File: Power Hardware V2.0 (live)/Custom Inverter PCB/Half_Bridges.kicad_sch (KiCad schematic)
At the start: 27 parts, among them Q1 CSD19532Q5B, Q2 CSD19532Q5B, Q3 CSD19532Q5B, Q4 CSD19532Q5B, Q5 CSD19532Q5B, Q6 CSD19532Q5B

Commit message: switches instead of relays. Short on half bridge fixed. encoder page made. root page connections fixed
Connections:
- net +100VDC: no longer C6.2, C7.2, C8.2, Q1.1, Q2.5_8, Q3.1, Q4.5_8, Q5.1, Q6.5_8, R5.2, R8.2, R9.2, TP1.TP, TP6.TP, TP9.TP
- new net GND: C6.2, C7.2, C8.2, R5.2, R8.2, R9.2
- new net MOTA: Q1.1, Q2.5_8, TP1.TP
- new net MOTB: Q3.1, Q4.5_8, TP6.TP
- new net MOTC: Q5.1, Q6.5_8, TP9.TP

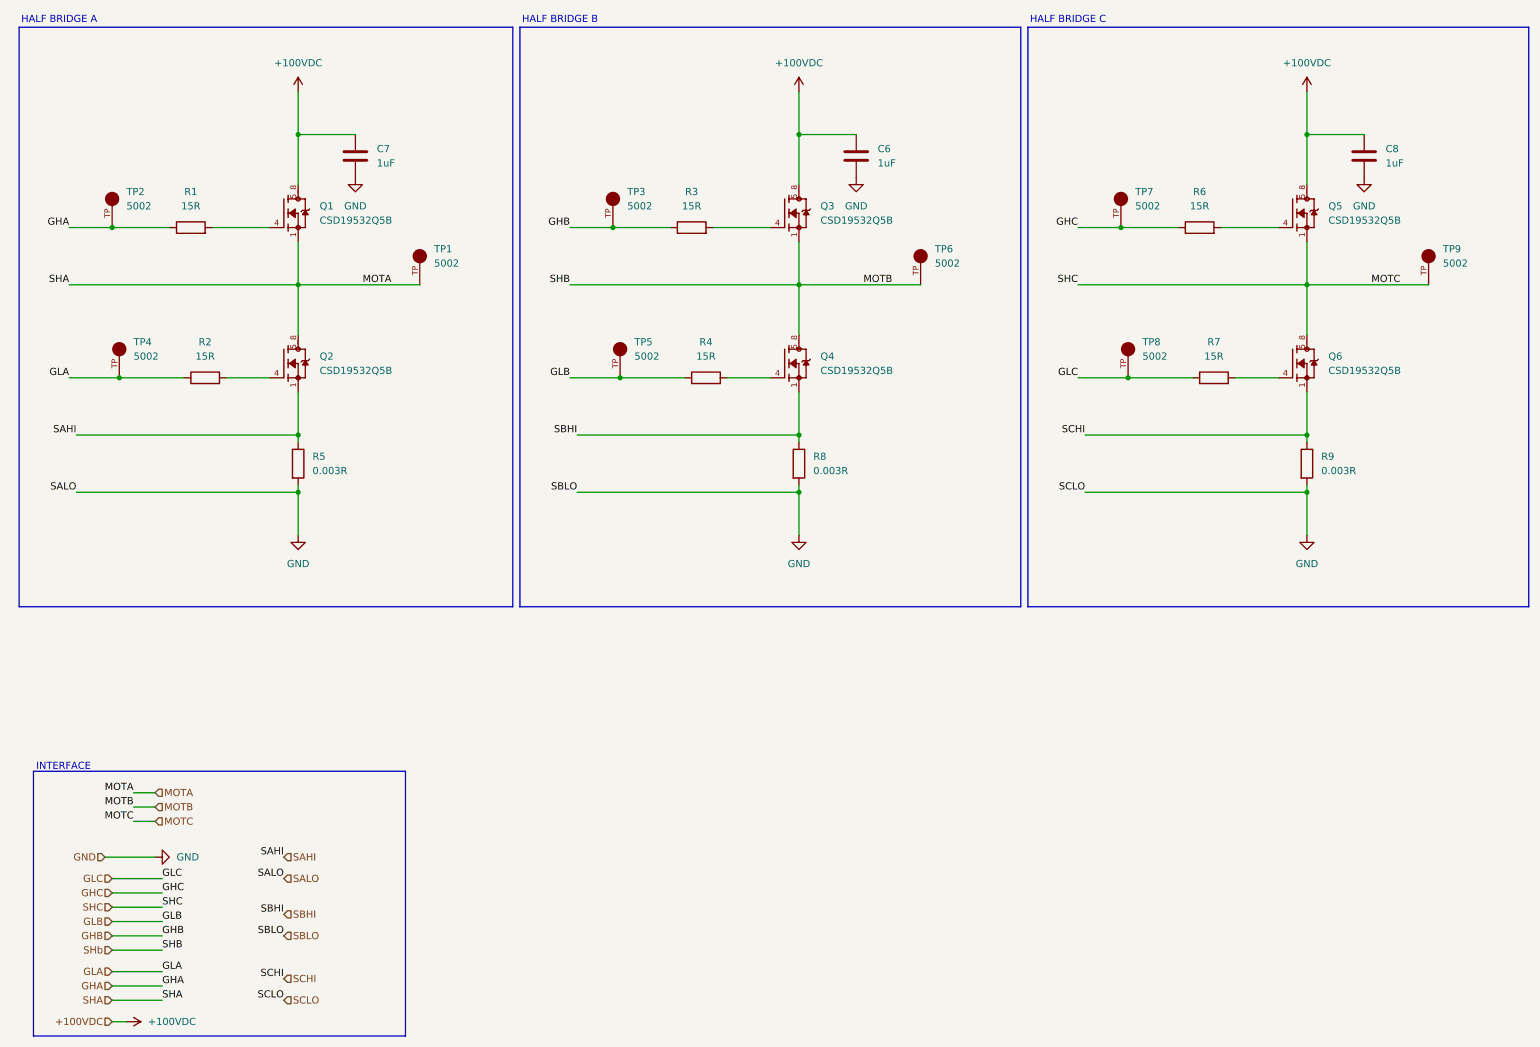
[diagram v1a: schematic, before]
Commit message: Schematic Changes
-Changed 3.3V regulator to a higher power unit for the sin-cos circuit (from 500mA to 3A)
-Fixed flipped MOTA,B,C connection to Output Terminal
- Current Sense IC setup
- Fuses for Phase current outputs
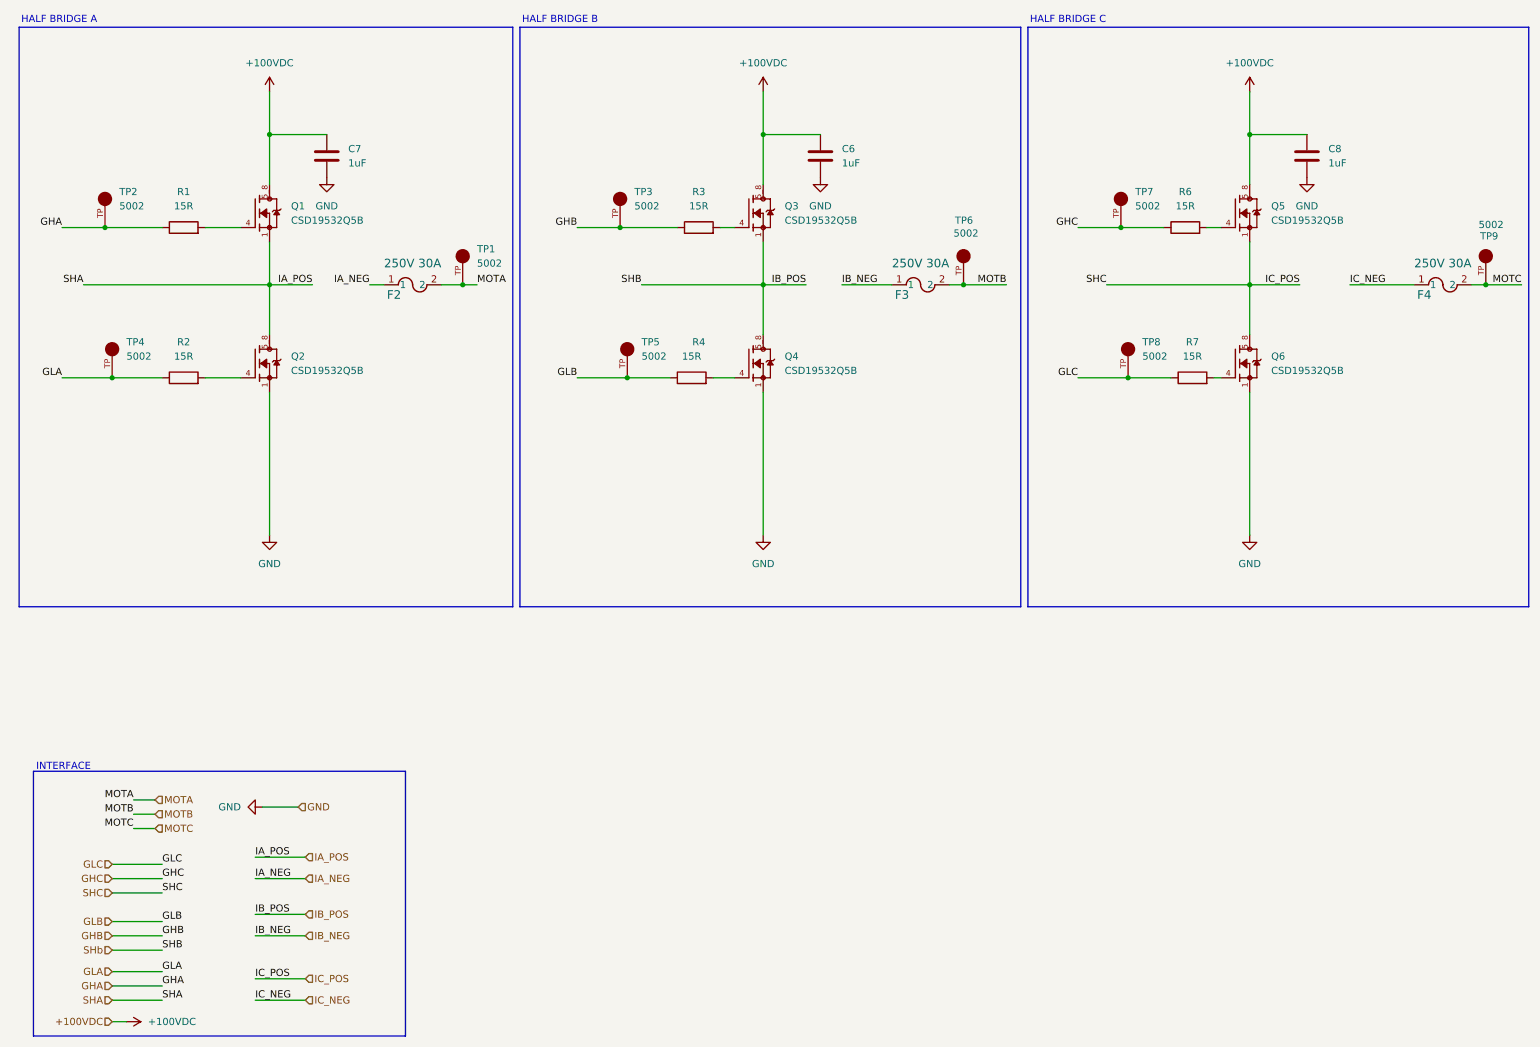
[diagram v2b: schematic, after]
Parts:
- removed R5, R8, R9: 0.003R, Resistor_SMD:R_2512_6332Metric, symbol Device:R
- added F2, F3, F4: 250V 30A, 0463030.ER:FUSE_0463_LTF, symbol 2025-02-24_21-09-15:0463030.ER
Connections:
- net SAHI is gone; now on net GND: Q2.1
- net SBHI is gone; now on net GND: Q4.1
- net SCHI is gone; now on net GND: Q6.1
- net MOTA: now also F2.2; no longer Q1.1, Q2.5_8
- net MOTB: now also F3.2; no longer Q3.1, Q4.5_8
- net MOTC: now also F4.2; no longer Q5.1, Q6.5_8
- new net IA_NEG: F2.1
- new net IA_POS: Q1.1, Q2.5_8
- new net IB_NEG: F3.1
- new net IB_POS: Q3.1, Q4.5_8
- new net IC_NEG: F4.1
- new net IC_POS: Q5.1, Q6.5_8
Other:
- moved on the sheet: C6, C7, C8, Q1, Q2, Q3, Q4, Q5, Q6, R1, R2, R3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

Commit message: no major changes
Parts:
- F2, F3, F4: footprint 0463030.ER:FUSE_0463_LTF -> 0463030ERFUSE:FUSE_0463_LTF-L
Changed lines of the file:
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@@
 			)
 		)
-		(property "Footprint" "0463030.ER:FUSE_0463_LTF"
+		(property "Footprint" "0463030ERFUSE:FUSE_0463_LTF-L"
 			(at 78.74 62.23 0)
 			(effects
@@
 			)
 		)
-		(property "Footprint" "0463030.ER:FUSE_0463_LTF"
+		(property "Footprint" "0463030ERFUSE:FUSE_0463_LTF-L"
 			(at 168.91 62.23 0)
 			(effects
@@
 			)
 		)
-		(property "Footprint" "0463030.ER:FUSE_0463_LTF"
+		(property "Footprint" "0463030ERFUSE:FUSE_0463_LTF-L"
 			(at 261.62 62.23 0)
 			(effects

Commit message: footprint lib fixes
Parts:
- F2, F3, F4: footprint 0463030ERFUSE:FUSE_0463_LTF-L -> 0463030_ER:FUSE_0463_LTF-M
- Q1, Q2, Q3, Q4, Q5, Q6: footprint CSD19532Q5B (1):TRANS_CSD19532Q5B -> CSD19532Q5B:TRANS_CSD19532Q5B
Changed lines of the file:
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@@
 			)
 		)
-		(property "Footprint" "0463030ERFUSE:FUSE_0463_LTF-L"
+		(property "Footprint" "0463030_ER:FUSE_0463_LTF-M"
 			(at 78.74 62.23 0)
 			(effects
@@
 			)
 		)
-		(property "Footprint" "CSD19532Q5B (1):TRANS_CSD19532Q5B"
+		(property "Footprint" "CSD19532Q5B:TRANS_CSD19532Q5B"
 			(at 55.88 76.2 0)
 			(effects
@@
 			)
 		)
-		(property "Footprint" "CSD19532Q5B (1):TRANS_CSD19532Q5B"
+		(property "Footprint" "CSD19532Q5B:TRANS_CSD19532Q5B"
 			(at 229.87 49.53 0)
 			(effects
@@
 			)
 		)
-		(property "Footprint" "0463030ERFUSE:FUSE_0463_LTF-L"
+		(property "Footprint" "0463030_ER:FUSE_0463_LTF-M"
 			(at 168.91 62.23 0)
 			(effects
@@
 			)
 		)
-		(property "Footprint" "CSD19532Q5B (1):TRANS_CSD19532Q5B"
+		(property "Footprint" "CSD19532Q5B:TRANS_CSD19532Q5B"
 			(at 229.87 76.2 0)
 			(effects
@@
 			)
 		)
-		(property "Footprint" "CSD19532Q5B (1):TRANS_CSD19532Q5B"
+		(property "Footprint" "CSD19532Q5B:TRANS_CSD19532Q5B"
 			(at 55.88 49.53 0)
 			(effects
@@
 			)
 		)
-		(property "Footprint" "CSD19532Q5B (1):TRANS_CSD19532Q5B"
+		(property "Footprint" "CSD19532Q5B:TRANS_CSD19532Q5B"
 			(at 143.51 76.2 0)
 			(effects
@@
 			)
 		)
-		(property "Footprint" "CSD19532Q5B (1):TRANS_CSD19532Q5B"
+		(property "Footprint" "CSD19532Q5B:TRANS_CSD19532Q5B"
 			(at 143.51 49.53 0)
 			(effects
@@
 			)
 		)
-		(property "Footprint" "0463030ERFUSE:FUSE_0463_LTF-L"
+		(property "Footprint" "0463030_ER:FUSE_0463_LTF-M"
 			(at 261.62 62.23 0)
 			(effects

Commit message: footprint fixes
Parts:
- TP1, TP2, TP3, TP4, TP5, TP6, TP7, TP8, TP9: footprint 5002 (1):KEYSTONE_5002 -> 5002:KEYSTONE_5002
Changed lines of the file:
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@@
 			)
 		)
-		(property "Footprint" "5002 (1):KEYSTONE_5002"
+		(property "Footprint" "5002:KEYSTONE_5002"
 			(at 274.32 57.15 0)
 			(effects
@@
 			)
 		)
-		(property "Footprint" "5002 (1):KEYSTONE_5002"
+		(property "Footprint" "5002:KEYSTONE_5002"
 			(at 92.71 57.15 0)
 			(effects
@@
 			)
 		)
-		(property "Footprint" "5002 (1):KEYSTONE_5002"
+		(property "Footprint" "5002:KEYSTONE_5002"
 			(at 30.48 73.66 0)
 			(effects
@@
 			)
 		)
-		(property "Footprint" "5002 (1):KEYSTONE_5002"
+		(property "Footprint" "5002:KEYSTONE_5002"
 			(at 209.55 46.99 0)
 			(effects
@@
 			)
 		)
-		(property "Footprint" "5002 (1):KEYSTONE_5002"
+		(property "Footprint" "5002:KEYSTONE_5002"
 			(at 29.21 46.99 0)
 			(effects
@@
 			)
 		)
-		(property "Footprint" "5002 (1):KEYSTONE_5002"
+		(property "Footprint" "5002:KEYSTONE_5002"
 			(at 121.92 73.66 0)
 			(effects
@@
 			)
 		)
-		(property "Footprint" "5002 (1):KEYSTONE_5002"
+		(property "Footprint" "5002:KEYSTONE_5002"
 			(at 181.61 57.15 0)
 			(effects
@@
 			)
 		)
-		(property "Footprint" "5002 (1):KEYSTONE_5002"
+		(property "Footprint" "5002:KEYSTONE_5002"
 			(at 210.82 73.66 0)
 			(effects
@@
 			)
 		)
-		(property "Footprint" "5002 (1):KEYSTONE_5002"
+		(property "Footprint" "5002:KEYSTONE_5002"
 			(at 120.65 46.99 0)
 			(effects

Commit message: PCB Fixes
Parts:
- Q1: footprint CSD19532Q5B:TRANS_CSD19532Q5B -> (none)
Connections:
- net GND: now also Q2.1_3, Q4.1_3, Q6.1_3; no longer Q2.1, Q4.1, Q6.1
- net IA_POS: now also Q1.1_3; no longer Q1.1
- net IB_POS: now also Q3.1_3; no longer Q3.1
- net IC_POS: now also Q5.1_3; no longer Q5.1
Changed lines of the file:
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@@
 	)
 	(symbol
+		(lib_name "CSD19532Q5B_1")
 		(lib_id "CSD19532Q5B:CSD19532Q5B")
 		(at 55.88 76.2 0)
@@
 		(pin "5_8"
 		)
-		(pin "1"
+		(pin "1_3"
 		)
 		(instances
@@
 		(pin "5_8"
 		)
-		(pin "1"
+		(pin "1_3"
 		)
 		(instances
@@
 		(pin "5_8"
 		)
-		(pin "1"
+		(pin "1_3"
 		)
 		(instances
@@
 			)
 		)
-		(property "Footprint" "CSD19532Q5B:TRANS_CSD19532Q5B"
+		(property "Footprint" ""
 			(at 55.88 49.53 0)
 			(effects
@@
 		(pin "5_8"
 		)
-		(pin "1"
+		(pin "1_3"
 		)
 		(instances
@@
 		(pin "5_8"
 		)
-		(pin "1"
+		(pin "1_3"
 		)
 		(instances
@@
 		(pin "5_8"
 		)
-		(pin "1"
-		)
-		(instances
+		(pin "1_3"
+		)
+		(instances
